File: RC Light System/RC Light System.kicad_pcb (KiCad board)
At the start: 2 copper layers, 34.3 x 41.3 mm, 21 parts, among them J1 OUTPUT 1, J10 BIND_IN, J2 OUTPUT 2, J3 THR_IN, J4 THR_OUT, J5 STR_IN, J6 STR_OUT, J7 AUX_IN, J8 AUX_OUT, J9 VBATT

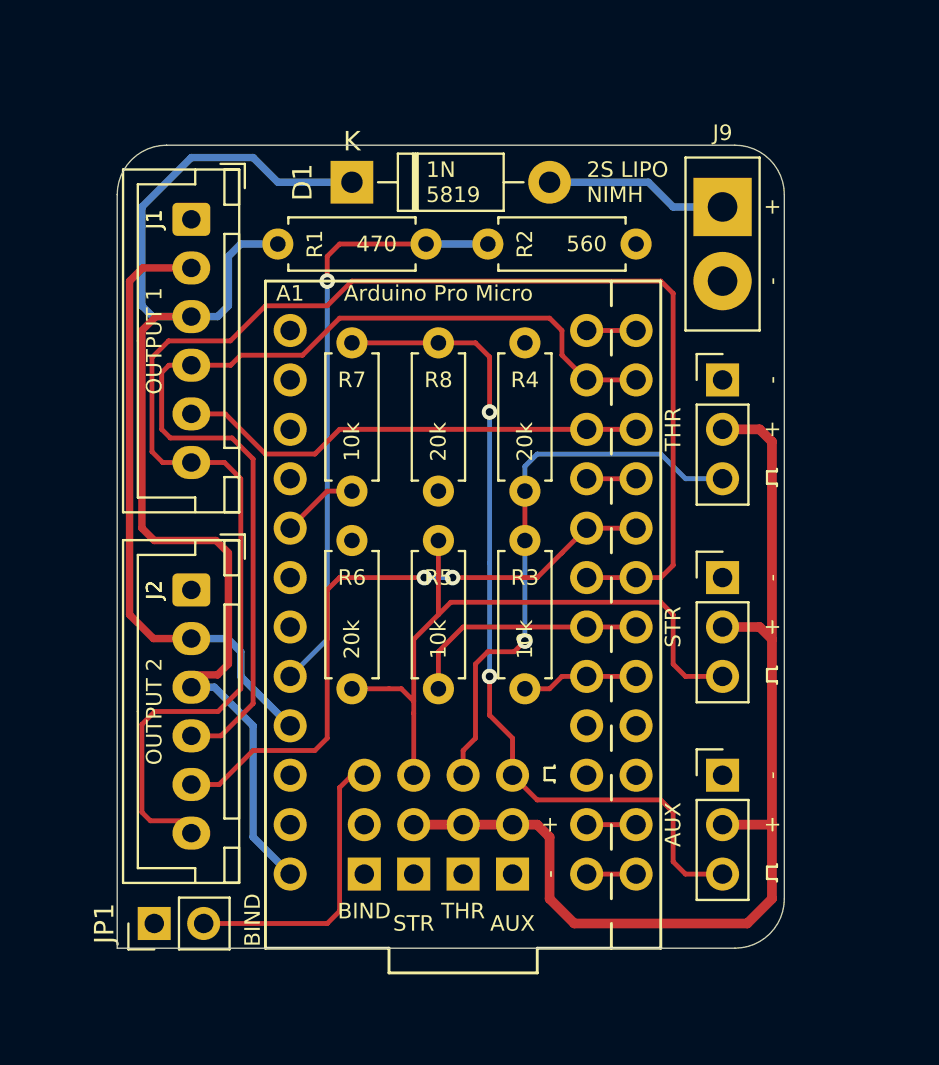
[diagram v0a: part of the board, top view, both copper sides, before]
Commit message: Simplified power to use 5/6v
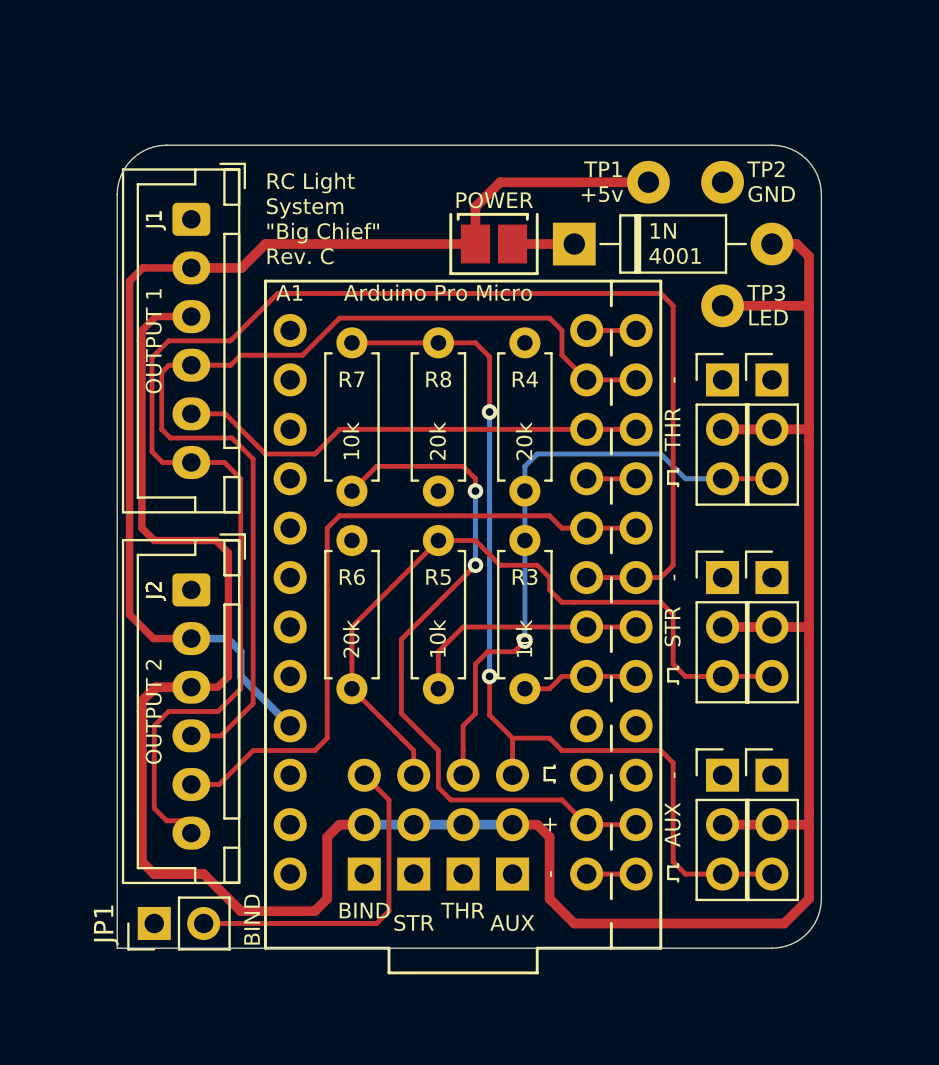
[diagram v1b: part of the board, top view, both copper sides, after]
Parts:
- removed R1: 470, resistor:R_Axial_DIN0207_L6.3mm_D2.5mm_P7.62mm_Horizontal
- removed R2: 560, resistor:R_Axial_DIN0207_L6.3mm_D2.5mm_P7.62mm_Horizontal
- added J11: STR_Y, Connector_PinHeader_2.54mm:PinHeader_1x03_P2.54mm_Vertical, F.Cu at (97.2, 103.5)
- added J12: AUX_Y, Connector_PinHeader_2.54mm:PinHeader_1x03_P2.54mm_Vertical, F.Cu at (97.2, 113.7)
- added JP2: POWER, solder_bridge:bridge, F.Cu at (83.8, 86.4)
- added TP1: +5v, rc_light_system:Testpoint, F.Cu at (90.8, 83.2)
- added TP2: GND, rc_light_system:Testpoint, F.Cu at (94.6, 83.2)
- added TP3: LED, rc_light_system:Testpoint, F.Cu at (94.6, 89.5)
- D1: value 1N5819 -> 1N4001
- J9: value VBATT -> THR_Y; footprint rc_light_system:Conn_Light_Power -> Connector_PinHeader_2.54mm:PinHeader_1x03_P2.54mm_Vertical
- moved D1 11.9 mm to (87.0, 86.4)
- moved J9 9.25 mm to (97.2, 93.3), turned to 0 degrees
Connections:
- net +5V renamed /+5v
- A1 pad 17: AUX -> (no net)
- A1 pad 2: Net-(A1-Pad2) -> AUX
- A1 pad 20: Net-(A1-Pad20) -> (no net)
- A1 pad 24: VCC -> (no net)
- D1 pad 1: VCC -> Net-(D1-Pad1)
- D1 pad 2: Net-(D1-Pad2) -> /+6v
- J1 pad 3: VCC -> /+6v
- J10 pad 2: (no net) -> /+6v
- J2 pad 3: VCC -> /+6v
- J3 pad 2: /BEC -> /+6v
- J4 pad 2: /BEC -> /+6v
- J5 pad 2: /BEC -> /+6v
- J6 pad 2: /BEC -> /+6v
- J7 pad 2: /BEC -> /+6v
- J8 pad 2: /BEC -> /+6v
- J9 pad 1: Net-(D1-Pad2) -> GND
- J9 pad 2: GND -> /+6v
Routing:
- net /+6v: track 0.00 -> 134.0 mm
- net VCC: track 65.9 -> 0.00 mm
- net /BEC: track 54.5 -> 0.00 mm
- net AUX: track 3.96 -> 36.3 mm, vias 0 -> 2
- net Net-(A1-Pad20): track 30.9 -> 0.00 mm, vias 1 -> 0
- net /+5v: track 32.0 -> 58.4 mm
- net Net-(D1-Pad2): track 9.42 -> 0.00 mm
- net Net-(J12-Pad3): track 43.8 -> 48.6 mm
- net Net-(D1-Pad1): track 0.00 -> 3.18 mm
- net Net-(J11-Pad3): track 34.0 -> 37.1 mm
- net Net-(A1-Pad2): track 2.54 -> 0.00 mm
- net Net-(J3-Pad3): track 28.9 -> 31.5 mm
- net /SER_CLK_2: track 32.8 -> 35.2 mm, vias 2 -> 0
- net /SER_LATCH: track 81.2 -> 78.9 mm
- net Net-(J10-Pad3): track 15.1 -> 17.3 mm
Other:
- board size 34.3 x 41.3 mm -> 36.2 x 41.3 mm
- board text added: "1N 4001"
- board text added: "RC Light System "Big Chief" Rev. C"
- board text removed: "1N 5819"
- board text removed: "2S LIPO NIMH"
- board text removed: "RC Light System "Big Chief" Rev. B"
